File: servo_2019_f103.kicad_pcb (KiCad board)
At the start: 2 copper layers, 45.1 x 86.4 mm, 22 parts, among them J1 Conn_01x20_Female, J3 Alim logique, J4 Conn_01x20_Female, Q1 PMF370XN, Q2 2N7000, Q4 PMF370XN, Q5 2N7000, U1 TC1262-33, U2 w5500, U3 servo_connector

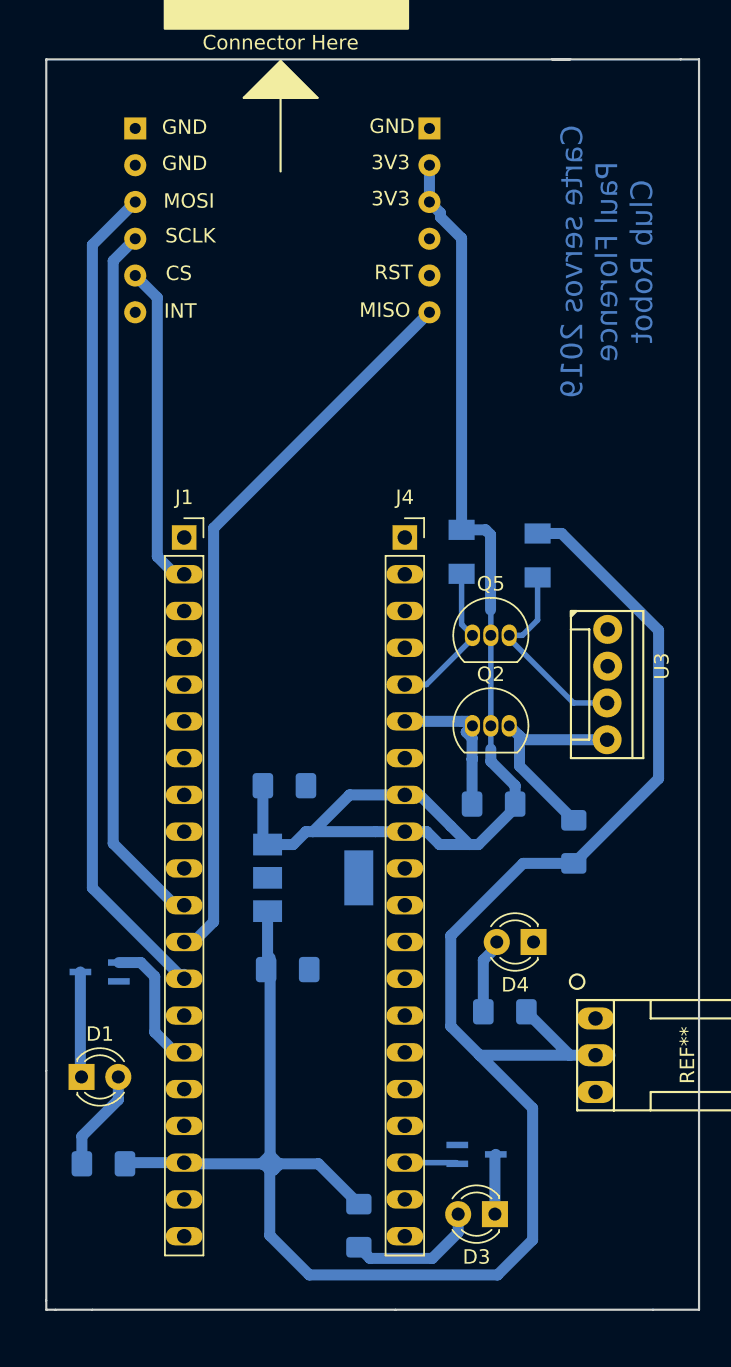
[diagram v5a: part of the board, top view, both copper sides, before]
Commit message: Fix wrong w5500 footprint
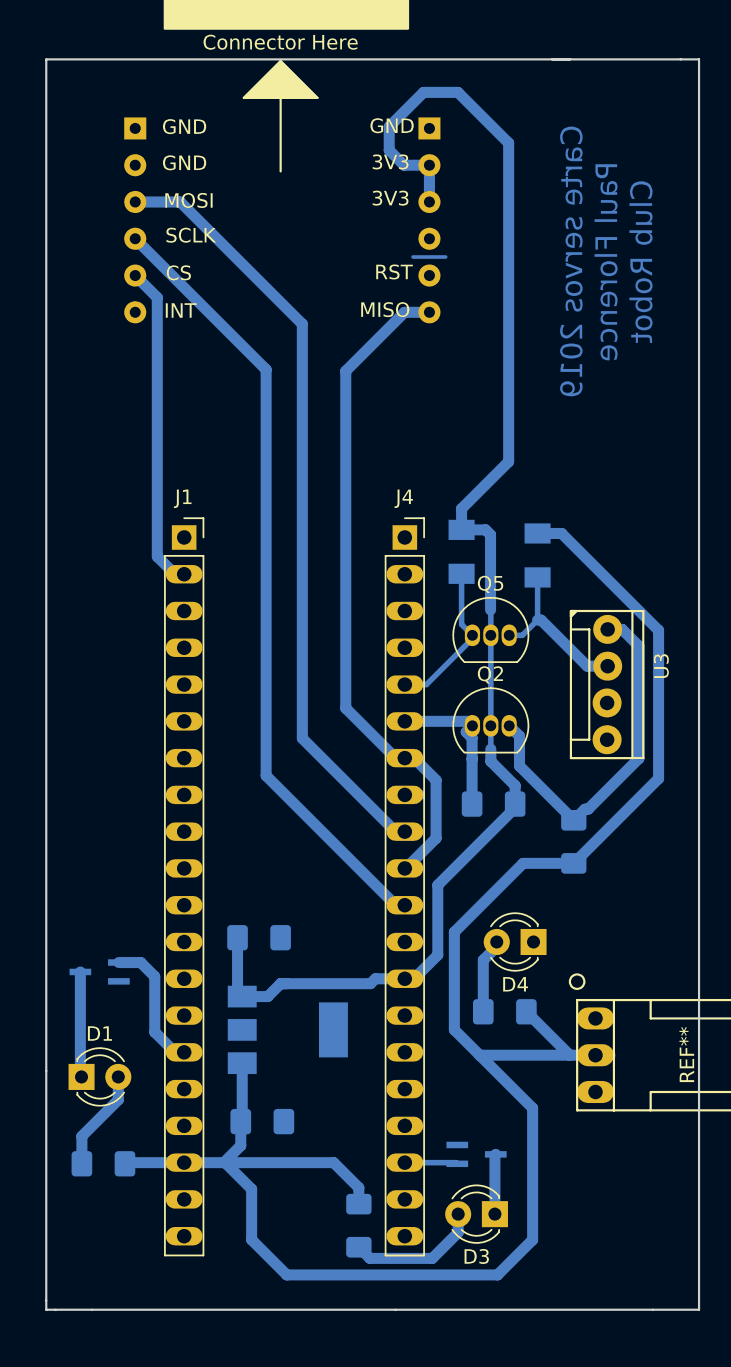
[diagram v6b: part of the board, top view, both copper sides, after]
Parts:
- moved C1 10.6 mm to (122.2, 119.1)
- moved C2 10.6 mm to (122.0, 106.4)
- moved U1 10.6 mm to (124.0, 112.8)
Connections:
- J1 pad 11: /sck -> Net-(J1-Pad11)
- J1 pad 12: /miso -> Net-(J1-Pad12)
- J1 pad 13: /mosi -> Net-(J1-Pad13)
- J4 pad 10: Net-(J4-Pad10) -> /miso
- J4 pad 11: GND -> /sck
- J4 pad 12: GND -> Net-(J4-Pad12)
- J4 pad 13: Net-(J4-Pad13) -> +3V3
- J4 pad 14: Net-(J4-Pad14) -> GND
- J4 pad 15: Net-(J4-Pad15) -> GND
- J4 pad 16: Net-(J4-Pad16) -> GND
- J4 pad 17: Net-(J4-Pad17) -> GND
- J4 pad 7: Net-(J4-Pad7) -> /miso
- J4 pad 8: +3V3 -> Net-(J4-Pad8)
- J4 pad 9: +3V3 -> /mosi
- U3 pad 1: Net-(U3-Pad1) -> /5V_logic_tx
- U3 pad 2: Net-(U3-Pad2) -> /5V_logic_rx
- U3 pad 3: /5V_logic_rx -> Net-(U3-Pad3)
- U3 pad 4: /5V_logic_tx -> Net-(U3-Pad4)
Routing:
- net +3V3: track 84.2 -> 99.6 mm
- net +5V: track 142.0 -> 131.2 mm
- net /5V_logic_tx: track 14.9 -> 25.0 mm
- net /sck: track 49.1 -> 54.1 mm
- net /miso: track 50.9 -> 46.1 mm
- net /mosi: track 57.9 -> 53.4 mm
- net /5V_logic_rx: track 14.2 -> 11.7 mm
- net GND: track 0.00 -> 2.25 mm
- net Net-(J4-Pad8): track 0.00 -> 1.02 mm
- net Net-(J4-Pad7): track 0.64 -> 0.00 mm

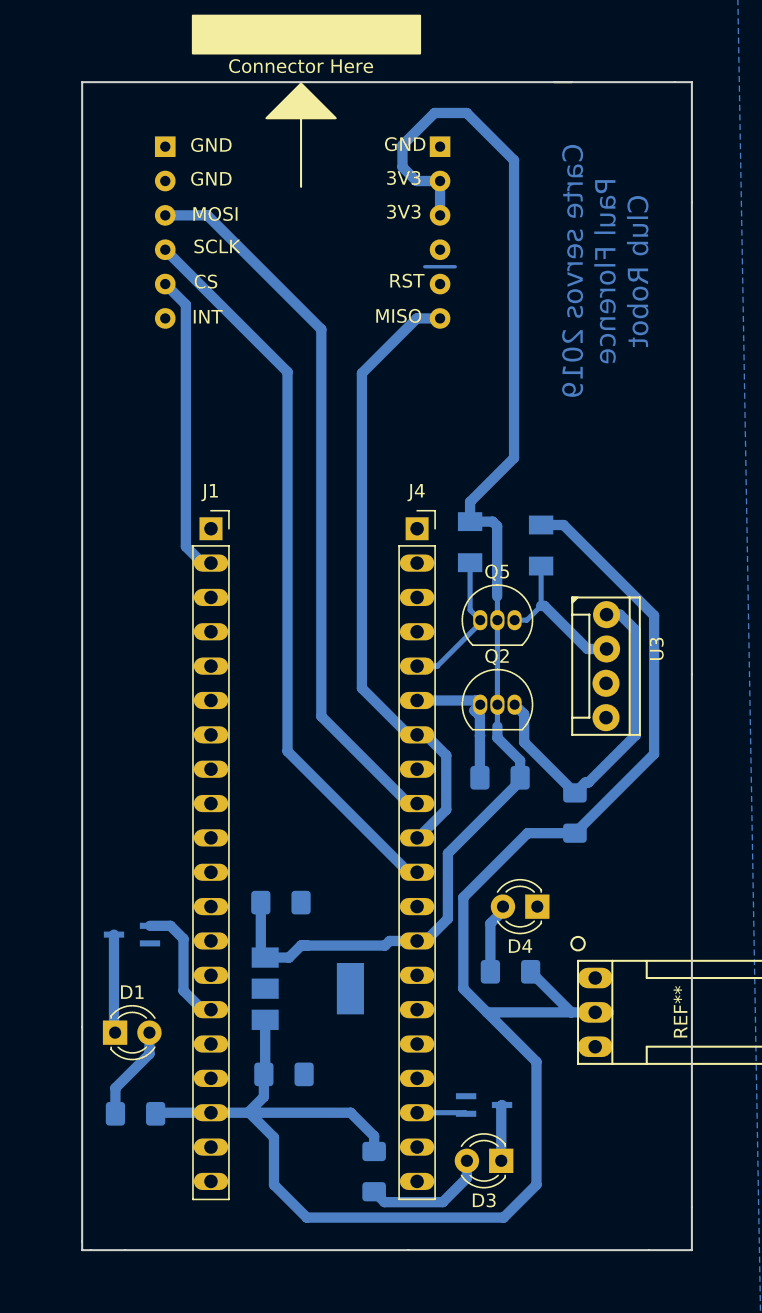
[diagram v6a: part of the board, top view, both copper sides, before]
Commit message: Add version number and drill hole on PCB
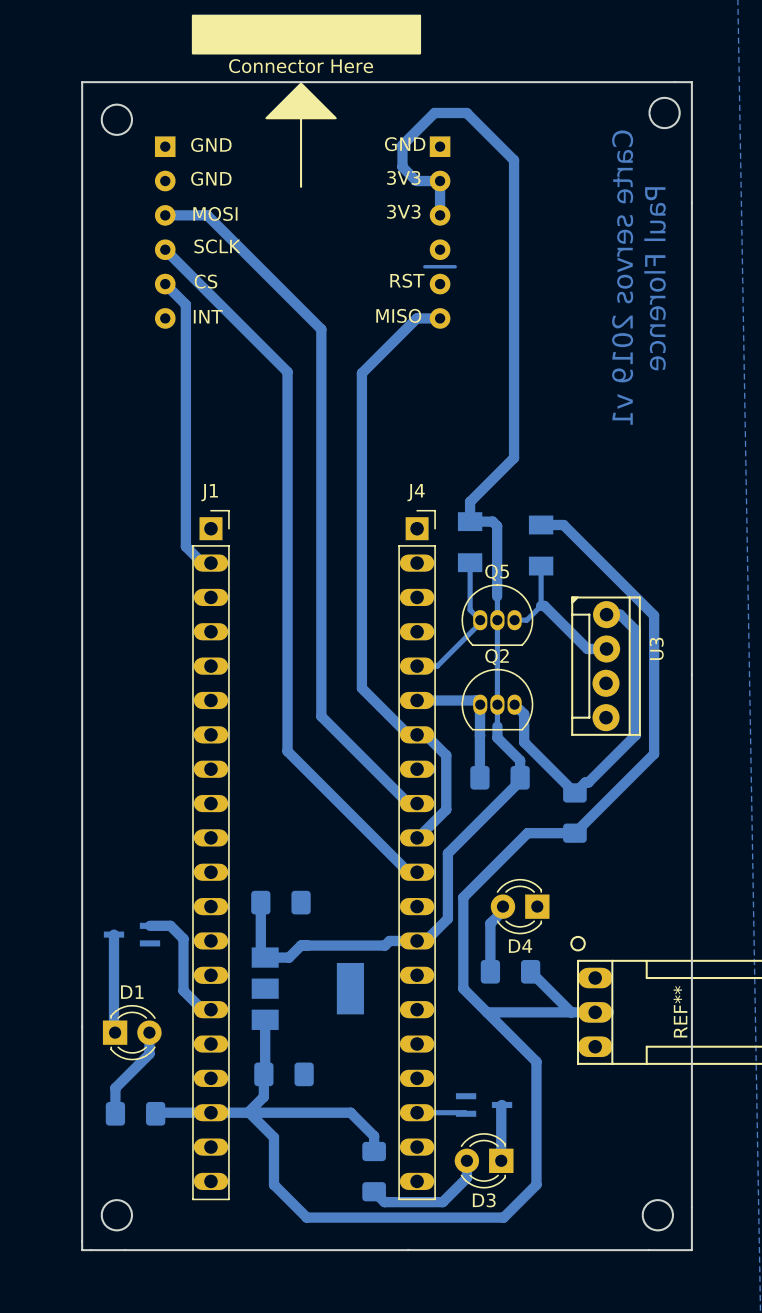
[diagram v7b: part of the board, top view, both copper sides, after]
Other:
- outline, holes or cut-outs redrawn
- board text added: "Carte servos 2019 v1 Paul Florence"
- board text removed: "Carte servos 2019 Paul Florence Club Robot"
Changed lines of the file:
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@@
-(kicad_pcb (version 20171130) (host pcbnew 5.0.2-bee76a0~70~ubuntu16.04.1)
+(kicad_pcb (version 20171130) (host pcbnew 5.1.1)
   (general
     (thickness 1.6)
-    (drawings 16)
-    (tracks 145)
+    (drawings 19)
+    (tracks 146)
     (zones 0)
     (modules 22)
@@
   )
   (setup
-    (last_trace_width 0.254)
+    (last_trace_width 0.762)
     (user_trace_width 0.254)
     (user_trace_width 0.381)
@@
     (zone_45_only no)
     (trace_min 0.2)
-    (segment_width 0.2)
-    (edge_width 0.15)
     (via_size 1.5)
     (via_drill 0.8)
@@
     (uvia_min_size 0.2)
     (uvia_min_drill 0.1)
+    (edge_width 0.15)
+    (segment_width 0.2)
     (pcb_text_width 0.3)
     (pcb_text_size 1.5 1.5)
@@
     )
   )
-  (gr_text "Carte servos 2019\nPaul Florence\nClub Robot" (at 146.05 59.69 90) (layer B.Cu)
+  (gr_circle (center 150.381967 48) (end 151.381967 47.5) (layer Edge.Cuts) (width 0.15))
+  (gr_circle (center 149.881967 129.5) (end 150.881967 129) (layer Edge.Cuts) (width 0.15))
+  (gr_circle (center 109.881967 129.5) (end 110.881967 129) (layer Edge.Cuts) (width 0.15))
+  (gr_circle (center 109.881967 48.5) (end 110.881967 48) (layer Edge.Cuts) (width 0.15))
+  (gr_text "Carte servos 2019 v1\nPaul Florence" (at 148.5392 60.2107 90) (layer B.Cu)
     (effects (font (size 1.5 1.5) (thickness 0.3)) (justify mirror))
   )
   (gr_line (start 152.4 45.72) (end 151.13 45.72) (layer Edge.Cuts) (width 0.15))
   (gr_line (start 152.4 54.61) (end 152.4 45.72) (layer Edge.Cuts) (width 0.15))
-  (gr_line (start 142.24 45.72) (end 151.13 45.72) (layer Edge.Cuts) (width 0.15))
   (gr_line (start 149.225 132.08) (end 152.4 132.08) (layer Edge.Cuts) (width 0.15))
   (gr_line (start 152.4 128.905) (end 152.4 132.08) (layer Edge.Cuts) (width 0.15))
@@
   (gr_line (start 152.4 89.535) (end 152.4 128.905) (layer Edge.Cuts) (width 0.15))
   (gr_line (start 152.4 89.535) (end 152.4 54.61) (layer Edge.Cuts) (width 0.15))
-  (gr_line (start 107.315 45.72) (end 143.51 45.72) (layer Edge.Cuts) (width 0.15))
+  (gr_line (start 107.315 45.72) (end 151.13 45.72) (layer Edge.Cuts) (width 0.15))
   (gr_line (start 107.315 115.57) (end 107.315 45.72) (layer Edge.Cuts) (width 0.15))
-  (segment (start 132.65 59.37) (end 134.9 59.37) (width 0.254) (layer B.Cu) (net 2))
   (segment (start 120.5 115.4) (end 120.85 115.05) (width 0.762) (layer B.Cu) (net 1) (status 30))
   (segment (start 117.475 121.92) (end 116.84 121.92) (width 0.762) (layer B.Cu) (net 1) (status 30))
@@
   (segment (start 121.5 127.25) (end 123.926357 129.676357) (width 0.762) (layer B.Cu) (net 1))
   (segment (start 123.926357 129.676357) (end 138.484143 129.676357) (width 0.762) (layer B.Cu) (net 1))
+  (segment (start 132.65 59.37) (end 134.9 59.37) (width 0.254) (layer B.Cu) (net 2))
   (segment (start 133.78 53.03) (end 133.78 55.57) (width 0.762) (layer B.Cu) (net 3) (status 30))
   (segment (start 137.662 78.215) (end 138 78.553) (width 0.762) (layer B.Cu) (net 3))
@@
   (segment (start 133.374398 48) (end 131 50.374398) (width 0.762) (layer B.Cu) (net 3))
   (segment (start 135.75 48) (end 133.374398 48) (width 0.762) (layer B.Cu) (net 3))
-  (segment (start 132.08 96.52) (end 133.096 96.52) (width 0.762) (layer B.Cu) (net 44) (status 30))
   (segment (start 109.67 115.92) (end 109.75 116) (width 0.762) (layer B.Cu) (net 4) (status 30))
   (segment (start 109.67 108.75) (end 109.67 115.92) (width 0.762) (layer B.Cu) (net 4) (status 30))
@@
   (segment (start 147.09 85.09) (end 148.25 86.25) (width 0.762) (layer B.Cu) (net 28))
   (segment (start 132.715 91.44) (end 132.08 91.44) (width 0.762) (layer B.Cu) (net 29) (status 30))
-  (segment (start 136.316847 92.183153) (end 136.73299 91.76701) (width 0.762) (layer B.Cu) (net 29) (status 30))
   (segment (start 136.44 91.44) (end 136.73299 91.73299) (width 0.762) (layer B.Cu) (net 29) (status 30))
   (segment (start 132.08 91.44) (end 136.44 91.44) (width 0.762) (layer B.Cu) (net 29) (status 30))
   (segment (start 136.725 94.053) (end 136.75 94.028) (width 0.762) (layer B.Cu) (net 29))
   (segment (start 136.725 97.155) (end 136.725 94.053) (width 0.762) (layer B.Cu) (net 29) (status 10))
-  (segment (start 136.725 92.591306) (end 136.316847 92.183153) (width 0.762) (layer B.Cu) (net 29) (status 20))
-  (segment (start 136.725 94.053) (end 136.725 92.591306) (width 0.762) (layer B.Cu) (net 29))
+  (segment (start 136.73299 92.508096) (end 136.73299 91.75) (width 0.762) (layer B.Cu) (net 29))
+  (segment (start 136.73299 93.76701) (end 136.73299 92.508096) (width 0.762) (layer B.Cu) (net 29))
+  (segment (start 136.725 94.053) (end 136.725 93.775) (width 0.762) (layer B.Cu) (net 29))
+  (segment (start 136.725 93.775) (end 136.73299 93.76701) (width 0.762) (layer B.Cu) (net 29))
   (segment (start 140.196 85.5) (end 139.29 85.5) (width 0.381) (layer B.Cu) (net 30) (status 20))
   (segment (start 141.25 84.446) (end 140.196 85.5) (width 0.381) (layer B.Cu) (net 30))
@@
   (segment (start 133.575 88.9) (end 136.75 85.725) (width 0.381) (layer B.Cu) (net 31) (status 20))
   (segment (start 132.08 88.9) (end 133.575 88.9) (width 0.381) (layer B.Cu) (net 31) (status 10))
+  (segment (start 132.715 93.98) (end 132.08 93.98) (width 0.762) (layer B.Cu) (net 32))
+  (segment (start 134.23901 95.50401) (end 132.715 93.98) (width 0.762) (layer B.Cu) (net 32))
+  (segment (start 134.23901 99.51166) (end 134.23901 95.50401) (width 0.762) (layer B.Cu) (net 32))
+  (segment (start 132.15067 101.6) (end 134.23901 99.51166) (width 0.762) (layer B.Cu) (net 32))
+  (segment (start 132.08 101.6) (end 132.15067 101.6) (width 0.762) (layer B.Cu) (net 32))
+  (segment (start 132.06 63.19) (end 133.78 63.19) (width 0.762) (layer B.Cu) (net 32))
+  (segment (start 128 67.25) (end 132.06 63.19) (width 0.762) (layer B.Cu) (net 32))
+  (segment (start 128 90.535) (end 128 67.25) (width 0.762) (layer B.Cu) (net 32))
+  (segment (start 132.08 93.98) (end 131.445 93.98) (width 0.762) (layer B.Cu) (net 32))
+  (segment (start 131.445 93.98) (end 128 90.535) (width 0.762) (layer B.Cu) (net 32))
   (segment (start 114.984001 62.174001) (end 113.46 60.65) (width 0.762) (layer B.Cu) (net 33) (status 20))
   (segment (start 114.984001 80.059001) (end 114.984001 62.174001) (width 0.762) (layer B.Cu) (net 33))
@@
   (segment (start 125 64) (end 116.57 55.57) (width 0.762) (layer B.Cu) (net 35))
   (segment (start 131.445 83.82) (end 132.08 83.82) (width 0.762) (layer B.Cu) (net 36) (status 30))
-  (segment (start 132.715 93.98) (end 132.08 93.98) (width 0.762) (layer B.Cu) (net 32))
-  (segment (start 134.23901 95.50401) (end 132.715 93.98) (width 0.762) (layer B.Cu) (net 32))
-  (segment (start 134.23901 99.51166) (end 134.23901 95.50401) (width 0.762) (layer B.Cu) (net 32))
-  (segment (start 132.15067 101.6) (end 134.23901 99.51166) (width 0.762) (layer B.Cu) (net 32))
-  (segment (start 132.08 101.6) (end 132.15067 101.6) (width 0.762) (layer B.Cu) (net 32))
-  (segment (start 132.06 63.19) (end 133.78 63.19) (width 0.762) (layer B.Cu) (net 32))
-  (segment (start 128 67.25) (end 132.06 63.19) (width 0.762) (layer B.Cu) (net 32))
-  (segment (start 128 90.535) (end 128 67.25) (width 0.762) (layer B.Cu) (net 32))
-  (segment (start 132.08 93.98) (end 131.445 93.98) (width 0.762) (layer B.Cu) (net 32))
-  (segment (start 131.445 93.98) (end 128 90.535) (width 0.762) (layer B.Cu) (net 32))
+  (segment (start 132.08 96.52) (end 133.096 96.52) (width 0.762) (layer B.Cu) (net 44) (status 30))
   (zone (net 2) (net_name GND) (layer B.Cu) (hatch edge 0.508)
     (connect_pads (clearance 0.508))
